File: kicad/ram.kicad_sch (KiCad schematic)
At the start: 85 parts, among them U20 74LS157, U21 74LS157, U22 TMS4164, U23 TMS4164, U24 TMS4164, U25 TMS4164, U26 TMS4164, U27 TMS4164, U28 TMS4164, U29 TMS4164, U30 TMS4164, U31 TMS4164, U32 TMS4164, U33 TMS4164, U34 TMS4164, U35 TMS4164, U36 TMS4164, U37 TMS4164, U38 TMS4164, U39 TMS4164, U40 TMS4164, U41 TMS4164, U42 TMS4164, U43 TMS4164, U44 TMS4164, U45 TMS4164, U46 TMS4164, U47 TMS4164, U48 TMS4164, U49 TMS4164, U50 TMS4164, U51 TMS4164, U52 TMS4164, U53 TMS4164, U54 TMS4164, U55 TMS4164, U56 TMS4164, U57 TMS4164, U62 74LS08, U75 PL16L8, U76 SN74LS280N

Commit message: update kicad project
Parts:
- removed C24: C_Bypass_5mm, seequa_footprints:C_Seequa_Bypass_Film_5mm, symbol seequa:C_Bypass_Film_2.54mm
- added C15, C24, C42: 0.1µF, seequa_footprints:C_Seequa_Bypass_Film_5mm, symbol Device:C_Small
- C10: seq_coord (none) -> C14
- C109: seq_coord (none) -> D8
- C11: seq_coord (none) -> C15
- C110: seq_coord (none) -> D10
- C114, RN6: seq_coord (none) -> C11
- C12, C13: seq_coord (none) -> C16
- C14: seq_coord (none) -> C17
- C16: seq_coord (none) -> C19
- C17, C18: seq_coord (none) -> C20
- C19: seq_coord (none) -> C21
- C20: seq_coord (none) -> C22
- C21: seq_coord (none) -> C23
- C22, C23: seq_coord (none) -> C24
- C25, U40, U41: seq_coord (none) -> B12
- C26, C27: seq_coord (none) -> B13
- C28: seq_coord (none) -> B14
- C29: seq_coord (none) -> B15
- C30, C31: seq_coord (none) -> B16
- C32: seq_coord (none) -> B17
- C33: seq_coord (none) -> K37
- C34: seq_coord (none) -> B19
- C35: seq_coord (none) -> B20
- C36, C37: seq_coord (none) -> B21
- C38: seq_coord (none) -> B22
- C39: seq_coord (none) -> B23
- C40, C41: seq_coord (none) -> B24
- C7, C8: seq_coord (none) -> C12
- C9: seq_coord (none) -> C13
- R6: seq_coord (none) -> B11
- R66, R67: seq_coord (none) -> D9
- R79: value ??Ω -> 300Ω; seq_coord (none) -> C10
- RN5: value 180 Ohms -> 180Ω; seq_coord (none) -> D13; seq_silkscreen RN7 -> (none)
- RN7: seq_coord (none) -> B10
- U20: value 74LS157 -> 74F157; seq_coord (none) -> C8; seq_notes (none) -> DRAM Address MUX 0; seq_silkscreen (none) -> F157
- U21: value 74LS157 -> 74F157; seq_coord (none) -> C9; seq_notes (none) -> DRAM Address Mux 1; seq_silkscreen (none) -> F157
- U22: seq_coord (none) -> C12; seq_silkscreen (none) -> 1
- U23: seq_coord (none) -> C12; seq_silkscreen (none) -> 2
- U24: seq_coord (none) -> C13; seq_silkscreen (none) -> 3
- U25: seq_coord (none) -> C14; seq_silkscreen (none) -> 4
- U26: seq_coord (none) -> C15; seq_silkscreen (none) -> 5
- U27: seq_coord (none) -> C16; seq_silkscreen (none) -> 6
- U28: seq_coord (none) -> C16; seq_silkscreen (none) -> 7
- U29: seq_coord (none) -> C17; seq_silkscreen (none) -> 8
- U30: seq_coord (none) -> C18; seq_silkscreen (none) -> 9
- U31: seq_coord (none) -> C19; seq_silkscreen (none) -> 19
- U32: seq_coord (none) -> C20; seq_silkscreen (none) -> 20
- U33: seq_coord (none) -> C21; seq_silkscreen (none) -> 21
- U34: seq_coord (none) -> C21; seq_silkscreen (none) -> 22
- U35: seq_coord (none) -> C22; seq_silkscreen (none) -> 23
- U36: seq_coord (none) -> C23; seq_silkscreen (none) -> 24
- U37: seq_coord (none) -> C24; seq_silkscreen (none) -> 25
- U38: seq_coord (none) -> C25; seq_silkscreen (none) -> 26
- U39: seq_coord (none) -> C25; seq_silkscreen (none) -> 27
- U42: seq_coord (none) -> B13; seq_silkscreen (none) -> 12
- U43: seq_coord (none) -> B14; seq_silkscreen (none) -> 13
- U44: seq_coord (none) -> B15; seq_silkscreen (none) -> 14
- U45: seq_coord (none) -> B16; seq_silkscreen (none) -> 15
- U46: seq_coord (none) -> B16; seq_silkscreen (none) -> 16
- U47: seq_coord (none) -> B17; seq_silkscreen (none) -> 17
- U48: seq_coord (none) -> B18; seq_silkscreen (none) -> 18
- U49: seq_coord (none) -> B19; seq_silkscreen (none) -> 28
- U50: seq_coord (none) -> B20; seq_silkscreen (none) -> 29
- U51: seq_coord (none) -> B21; seq_silkscreen (none) -> 30
- U52: seq_coord (none) -> B21; seq_silkscreen (none) -> 31
- U53: seq_coord (none) -> B22; seq_silkscreen (none) -> 32
- U54: seq_coord (none) -> B23; seq_silkscreen (none) -> 33
- U55: seq_coord (none) -> B24; seq_silkscreen (none) -> 34
- U56: seq_coord (none) -> B25; seq_silkscreen (none) -> 35
- U57: seq_coord (none) -> B25; seq_silkscreen (none) -> 36
- U62: seq_coord (none) -> B10; seq_silkscreen (none) -> LS08
- U75: value PL16L8 -> PAL16L8; seq_coord (none) -> D12; seq_notes RAM Bank Decoder -> DRAM Control PAL
- U76: seq_coord (none) -> B11; seq_notes (none) -> Parity Calculator
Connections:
- net +5V: now also U20.16 (VCC), U21.16 (VCC), C15.1, C24.1, C42.1; no longer U40.16 (VSS), U41.16 (VSS), U42.16 (VSS), U43.16 (VSS), U44.16 (VSS), U45.16 (VSS), U46.16 (VSS), U47.16 (VSS), U48.16 (VSS), U49.16 (VSS), U50.16 (VSS), U51.16 (VSS), U52.16 (VSS), U53.16 (VSS), U54.16 (VSS), U55.16 (VSS), U56.16 (VSS), U57.16 (VSS)
- net GND: now also U40.16 (VSS), U41.16 (VSS), U42.16 (VSS), U43.16 (VSS), U44.16 (VSS), U45.16 (VSS), U46.16 (VSS), U47.16 (VSS), U48.16 (VSS), U49.16 (VSS), U50.16 (VSS), U51.16 (VSS), U52.16 (VSS), U53.16 (VSS), U54.16 (VSS), U55.16 (VSS), U56.16 (VSS), U57.16 (VSS), C15.2, C24.2, C42.2
- net MD8: now also R6.1; no longer U76.4 (I)
- net ~{CAS_{0}}: now also U22.15 (~{CAS}), U23.15 (~{CAS}), U24.15 (~{CAS}), U25.15 (~{CAS}), U26.15 (~{CAS}), U27.15 (~{CAS}), U28.15 (~{CAS}), U29.15 (~{CAS}), U30.15 (~{CAS})
- net ~{CAS_{1}}: now also U40.15 (~{CAS}), U41.15 (~{CAS}), U42.15 (~{CAS}), U43.15 (~{CAS}), U44.15 (~{CAS}), U45.15 (~{CAS}), U46.15 (~{CAS}), U47.15 (~{CAS}), U48.15 (~{CAS})
- net ~{RAS_{1}}: no longer U38.4 (~{RAS})
- net ~{WR_{t}}: now also C114.1, R79.2, U75.8 (I_{7}); no longer RN5.1 (R1.1), U22.3 (~{WRITE}), U23.3 (~{WRITE}), U24.3 (~{WRITE}), U25.3 (~{WRITE}), U26.3 (~{WRITE}), U27.3 (~{WRITE}), U28.3 (~{WRITE}), U29.3 (~{WRITE}), U30.3 (~{WRITE}), U31.3 (~{WRITE}), U32.3 (~{WRITE}), U33.3 (~{WRITE}), U34.3 (~{WRITE}), U35.3 (~{WRITE}), U36.3 (~{WRITE}), U37.3 (~{WRITE}), U38.3 (~{WRITE}), U39.3 (~{WRITE}), U40.3 (~{WRITE}), U41.3 (~{WRITE}), U42.3 (~{WRITE}), U43.3 (~{WRITE}), U44.3 (~{WRITE}), U45.3 (~{WRITE}), U46.3 (~{WRITE}), U47.3 (~{WRITE}), U48.3 (~{WRITE}), U49.3 (~{WRITE}), U50.3 (~{WRITE}), U51.3 (~{WRITE}), U52.3 (~{WRITE}), U53.3 (~{WRITE}), U54.3 (~{WRITE}), U55.3 (~{WRITE}), U56.3 (~{WRITE}), U57.3 (~{WRITE}), U62.10, U62.12, U62.9
- net ~{WR}: now also RN5.15 (R2.2)
- net RAS/~{CAS}: now reaches C109.1, R66.1
- net RAS/~{CAS}: now also U20.1 (S), U21.1 (S), U62.1, U62.2
- net ~{RAS_{2}}: now reaches U41.4 (~{RAS})
- net ~{RAS_{2}}: now also RN5.5 (R5.1), U40.4 (~{RAS}), U42.4 (~{RAS}), U43.4 (~{RAS}), U44.4 (~{RAS}), U45.4 (~{RAS}), U46.4 (~{RAS}), U47.4 (~{RAS}), U48.4 (~{RAS})
- net ~{RAS_{3}}: now reaches U56.4 (~{RAS})
- net ~{RAS_{3}}: now also RN5.14 (R3.2), U49.4 (~{RAS}), U50.4 (~{RAS}), U51.4 (~{RAS}), U52.4 (~{RAS}), U53.4 (~{RAS}), U54.4 (~{RAS}), U55.4 (~{RAS}), U57.4 (~{RAS})
- net ~{WR_{1}}: now reaches RN5.2 (R2.1)
- net ~{WR_{1}}: now also U40.3 (~{WRITE}), U41.3 (~{WRITE}), U42.3 (~{WRITE}), U43.3 (~{WRITE}), U44.3 (~{WRITE}), U45.3 (~{WRITE}), U46.3 (~{WRITE}), U47.3 (~{WRITE}), U48.3 (~{WRITE}), U49.3 (~{WRITE}), U50.3 (~{WRITE}), U51.3 (~{WRITE}), U52.3 (~{WRITE}), U53.3 (~{WRITE}), U54.3 (~{WRITE}), U55.3 (~{WRITE}), U56.3 (~{WRITE}), U57.3 (~{WRITE})
- net ~{CAS}: now reaches RN5.7 (R7.1), RN5.8 (R8.1), U75.14 (I/~{O_{3}})
- net ~{RAS_{3}'}: now reaches RN5.3 (R3.1)
- net ~{RAS_{3}'}: now also U75.15 (I/~{O_{4}})
- net ~{PARITY_CLK}: now reaches U75.13 (I/~{O_{2}})
- net ~{RAS_{2}'}: now reaches U75.16 (I/~{O_{5}})
- net ~{RAS_{2}'}: now also RN5.12 (R5.2)
- net DATA_DIR: now reaches U75.19 (~{O_{8}})
- removed net MUX_SEL: R66.2, U20.1 (S), U21.1 (S), U62.1, U62.2, U75.12 (~{O_{1}})
- net PARITY_1 renamed PARITY_BIT
- net PARITY_BIT: now also U76.4 (I)
- net ROM_PAD renamed XA9
- new net RAS/~{CAS}': R66.2, U75.12 (~{O_{1}})
- new net ~{WR_{0}}: RN5.1 (R1.1), U22.3 (~{WRITE}), U23.3 (~{WRITE}), U24.3 (~{WRITE}), U25.3 (~{WRITE}), U26.3 (~{WRITE}), U27.3 (~{WRITE}), U28.3 (~{WRITE}), U29.3 (~{WRITE}), U30.3 (~{WRITE}), U31.3 (~{WRITE}), U32.3 (~{WRITE}), U33.3 (~{WRITE}), U34.3 (~{WRITE}), U35.3 (~{WRITE}), U36.3 (~{WRITE}), U37.3 (~{WRITE}), U38.3 (~{WRITE}), U39.3 (~{WRITE}), U62.10, U62.12, U62.9
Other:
- note added: "From ROM (Page 4)"
- note added: "To Data Buffer U19 (Page 3)"
- note added: "~{WR} retermination"
- moved on the sheet: C10, C11, C114, C12, C13, C14, C16, C17, C18, C19, C20, C21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

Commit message: More updates
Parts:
- R66: value ??Ω -> 56Ω; seq_notes (none) -> Green, Blue, Black, Gold
- R67: value ??Ω -> 300Ω; seq_notes (none) -> Orange, Black, Brown, Gold
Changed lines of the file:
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@@
 		)
 	)
-	(text_box "Like the IBM PC, the Chameleon stores even parity bits.\n\nWhen writing, the parity bit input to the parity generator is forced to 0. The even parity result calculated from bits 0-7 is driven to data bit 8 to be stored.\n\nWhen reading, the parity bit D8 is included in the parity calculation. The parity bit should always be 1, flipping the result of the calculation to odd parity. \n\nThus an asserted EVEN_PARITY signal during a read operation may be considered a parity error.\n\n\n"
+	(text_box "Like the IBM PC, the Chameleon stores even parity bits in the 9th DRAM chip (bit D8)\n\nWhen writing, the parity bit input to the parity generator is forced to 0. The even parity result calculated from bits 0-7 is driven to data bit 8 to be stored.\n\nWhen reading, the parity bit D8 is included in the parity calculation, flipping the result of the calculation to odd parity. \n\nThus, an asserted EVEN_PARITY signal during a read operation may be considered a parity error.\n\n\n"
 		(exclude_from_sim no)
 		(at 245.11 336.55 0)
@@
 	)
 	(junction
-		(at 194.31 39.37)
-		(diameter 0)
-		(color 0 194 0 1)
-	)
-	(junction
 		(at 412.75 383.54)
 		(diameter 0)
@@
 	)
 	(bus_entry
-		(at 194.31 316.23)
+		(at 194.31 321.31)
 		(size -2.54 2.54)
 		(stroke
@@
 	(wire
 		(pts
-			(xy 171.45 318.77) (xy 171.45 346.71)
+			(xy 171.45 323.85) (xy 171.45 346.71)
 		)
 		(stroke
@@
 	(wire
 		(pts
-			(xy 171.45 318.77) (xy 191.77 318.77)
+			(xy 171.45 323.85) (xy 191.77 323.85)
 		)
 		(stroke
@@
 	(bus
 		(pts
-			(xy 194.31 316.23) (xy 194.31 326.39)
+			(xy 194.31 321.31) (xy 194.31 326.39)
 		)
 		(stroke
@@
 		)
 	)
+	(bus
+		(pts
+			(xy 194.31 316.23) (xy 194.31 321.31)
+		)
+		(stroke
+			(width 0.75)
+			(type default)
+			(color 0 194 0 1)
+		)
+	)
 	(wire
 		(pts
@@
 	(bus
 		(pts
-			(xy 156.21 39.37) (xy 194.31 39.37)
-		)
-		(stroke
-			(width 0.75)
-			(type default)
-			(color 0 194 0 1)
-		)
-	)
-	(bus
-		(pts
 			(xy 279.4 72.39) (xy 279.4 74.93)
 		)
@@
 	)
 	(label "MD8"
-		(at 179.07 318.77 0)
+		(at 179.07 323.85 0)
 		(effects
 			(font
@@
 	)
 	(label "MD8"
-		(at 228.6 318.77 0)
+		(at 200.66 318.77 0)
 		(effects
 			(font
@@
 		)
 	)
-	(hierarchical_label "MD[0..8]"
-		(shape bidirectional)
-		(at 156.21 39.37 180)
-		(effects
-			(font
-				(size 1.27 1.27)
-			)
-			(justify right)
-		)
-	)
 	(hierarchical_label "XA[0..19]"
 		(shape input)
@@
 			)
 		)
-		(property "Value" "??Ω"
-			(at 57.912 59.69 90)
+		(property "Value" "300Ω"
+			(at 59.69 59.182 90)
 			(effects
 				(font
 					(size 1.27 1.27)
 				)
-				(justify left)
 			)
 		)
@@
 			)
 		)
-		(property "seq_notes" ""
+		(property "seq_notes" "Orange, Black, Brown, Gold"
+			(at 59.69 57.15 0)
+			(effects
+				(font
+					(size 1.27 1.27)
+				)
+				(hide yes)
+			)
+		)
+		(property "seq_port" ""
 			(at 59.69 57.15 0)
 			(effects
@@
 			)
 		)
-		(property "Value" "??Ω"
+		(property "Value" "56Ω"
 			(at 89.408 70.612 0)
 			(effects
@@
 			)
 		)
-		(property "seq_notes" ""
+		(property "seq_notes" "Green, Blue, Black, Gold"
+			(at 87.63 69.85 0)
+			(effects
+				(font
+					(size 1.27 1.27)
+				)
+				(hide yes)
+			)
+		)
+		(property "seq_port" ""
 			(at 87.63 69.85 0)
 			(effects

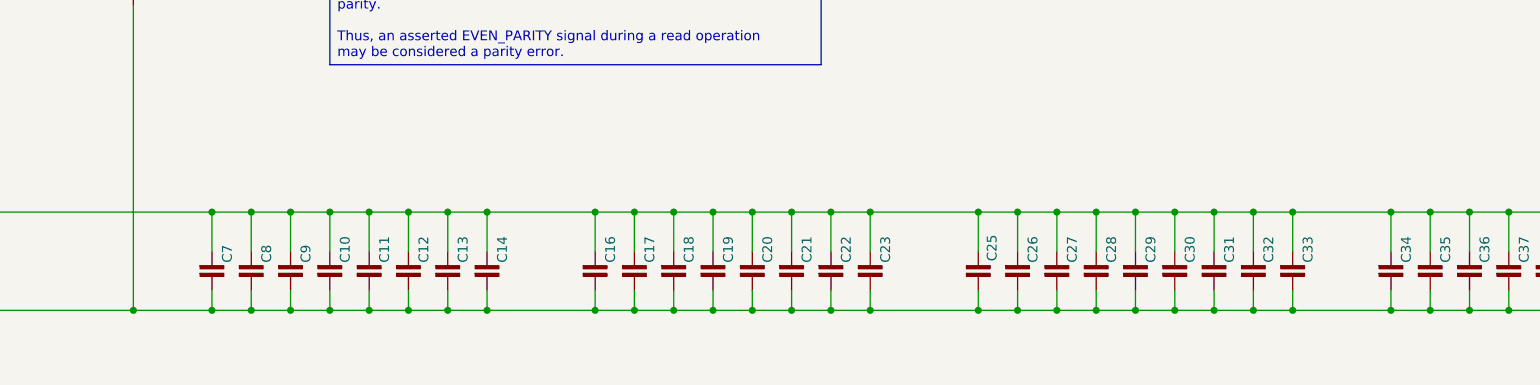
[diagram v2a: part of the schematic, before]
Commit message: Add parallel port, game port
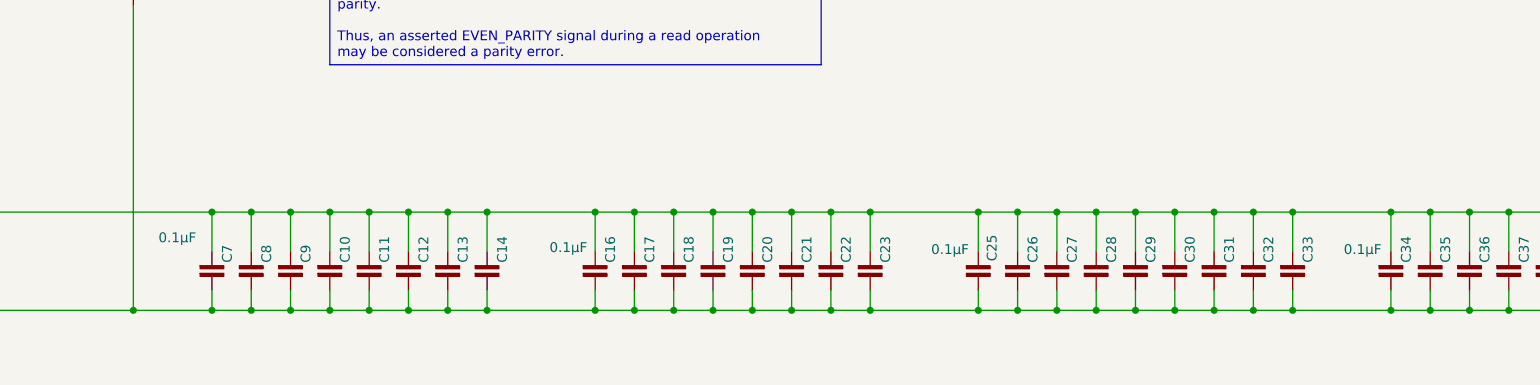
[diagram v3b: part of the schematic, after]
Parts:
- C16, C25, C34, C7: value C_Bypass_5mm -> 0.1µF
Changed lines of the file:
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@@
 			)
 		)
-		(property "Value" "C_Bypass_5mm"
-			(at 382.524 393.192 0)
+		(property "Value" "0.1µF"
+			(at 376.174 388.366 0)
 			(effects
 				(font
@@
 				)
 				(justify left)
-				(hide yes)
 			)
 		)
@@
 			)
 		)
+		(property "seq_port" ""
+			(at 382.27 391.16 0)
+			(effects
+				(font
+					(size 1.27 1.27)
+				)
+				(hide yes)
+			)
+		)
 		(pin "2"
 		)
@@
 			)
 		)
-		(property "Value" "C_Bypass_5mm"
-			(at 329.184 393.192 0)
+		(property "Value" "0.1µF"
+			(at 322.834 388.366 0)
 			(effects
 				(font
@@
 				)
 				(justify left)
-				(hide yes)
 			)
 		)
@@
 			)
 		)
+		(property "seq_port" ""
+			(at 328.93 391.16 0)
+			(effects
+				(font
+					(size 1.27 1.27)
+				)
+				(hide yes)
+			)
+		)
 		(pin "2"
 		)
@@
 			)
 		)
-		(property "Value" "C_Bypass_5mm"
-			(at 230.124 393.192 0)
+		(property "Value" "0.1µF"
+			(at 227.838 386.842 0)
 			(effects
 				(font
 					(size 1.27 1.27)
 				)
-				(justify left)
-				(hide yes)
+				(justify right)
 			)
 		)
@@
 			)
 		)
+		(property "seq_port" ""
+			(at 229.87 391.16 0)
+			(effects
+				(font
+					(size 1.27 1.27)
+				)
+				(hide yes)
+			)
+		)
 		(pin "2"
 		)
@@
 			)
 		)
-		(property "Value" "C_Bypass_5mm"
-			(at 279.654 393.192 0)
+		(property "Value" "0.1µF"
+			(at 278.384 388.112 0)
 			(effects
 				(font
 					(size 1.27 1.27)
 				)
-				(justify left)
-				(hide yes)
+				(justify right)
 			)
 		)
@@
 			(at 279.4 391.16 0)
 			(effects
+				(font
+					(size 1.27 1.27)
+				)
+				(hide yes)
+			)
+		)
+		(property "seq_port" ""
+			(at 279.4 391.16 0)
+			(effects
